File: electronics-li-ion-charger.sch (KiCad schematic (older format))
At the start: 16 parts

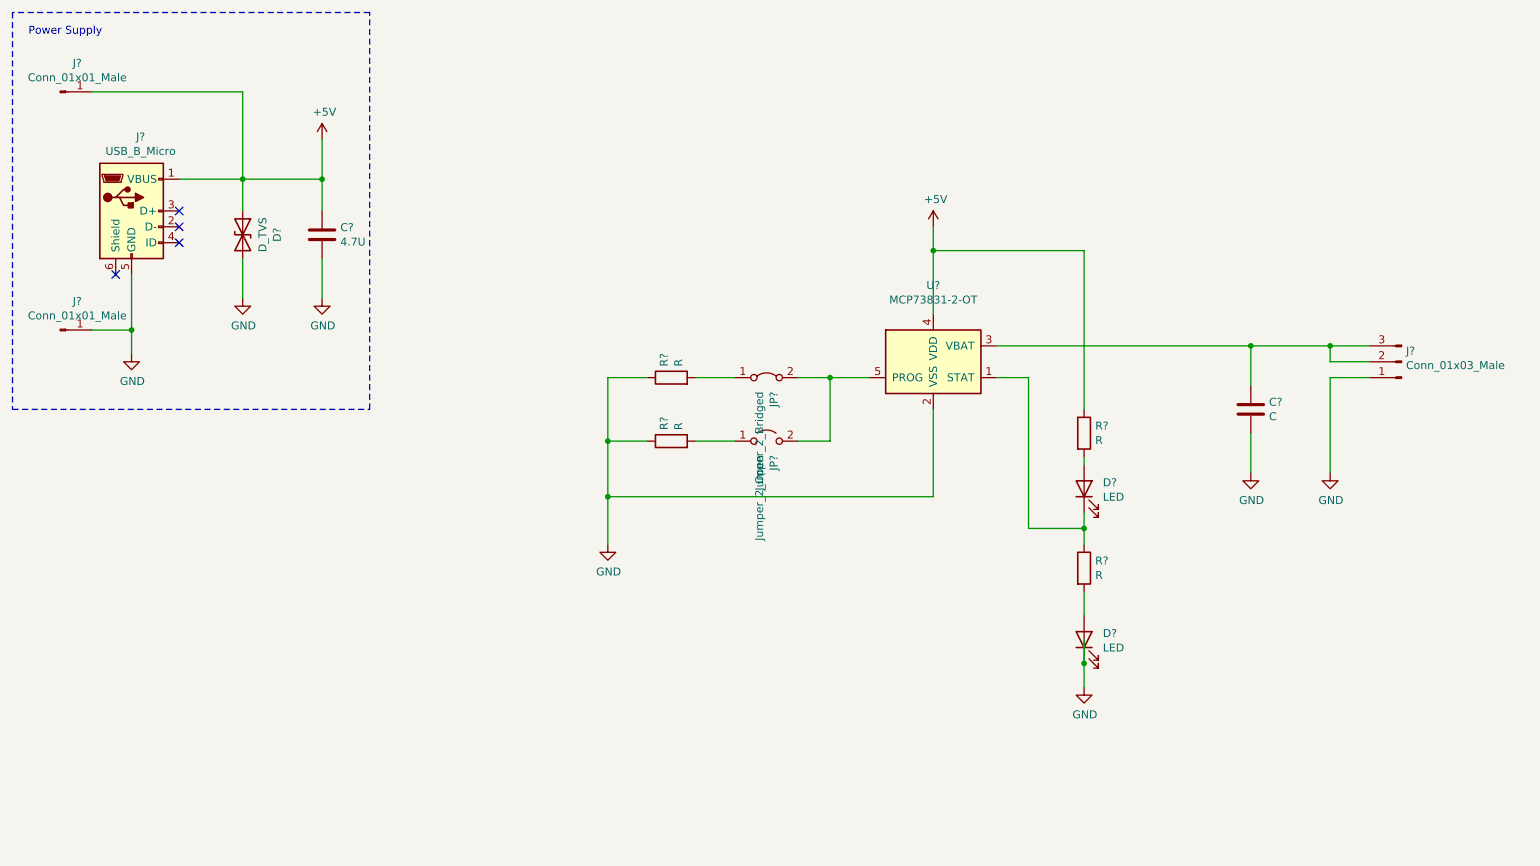
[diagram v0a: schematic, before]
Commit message: Complete charge current selection schematic.
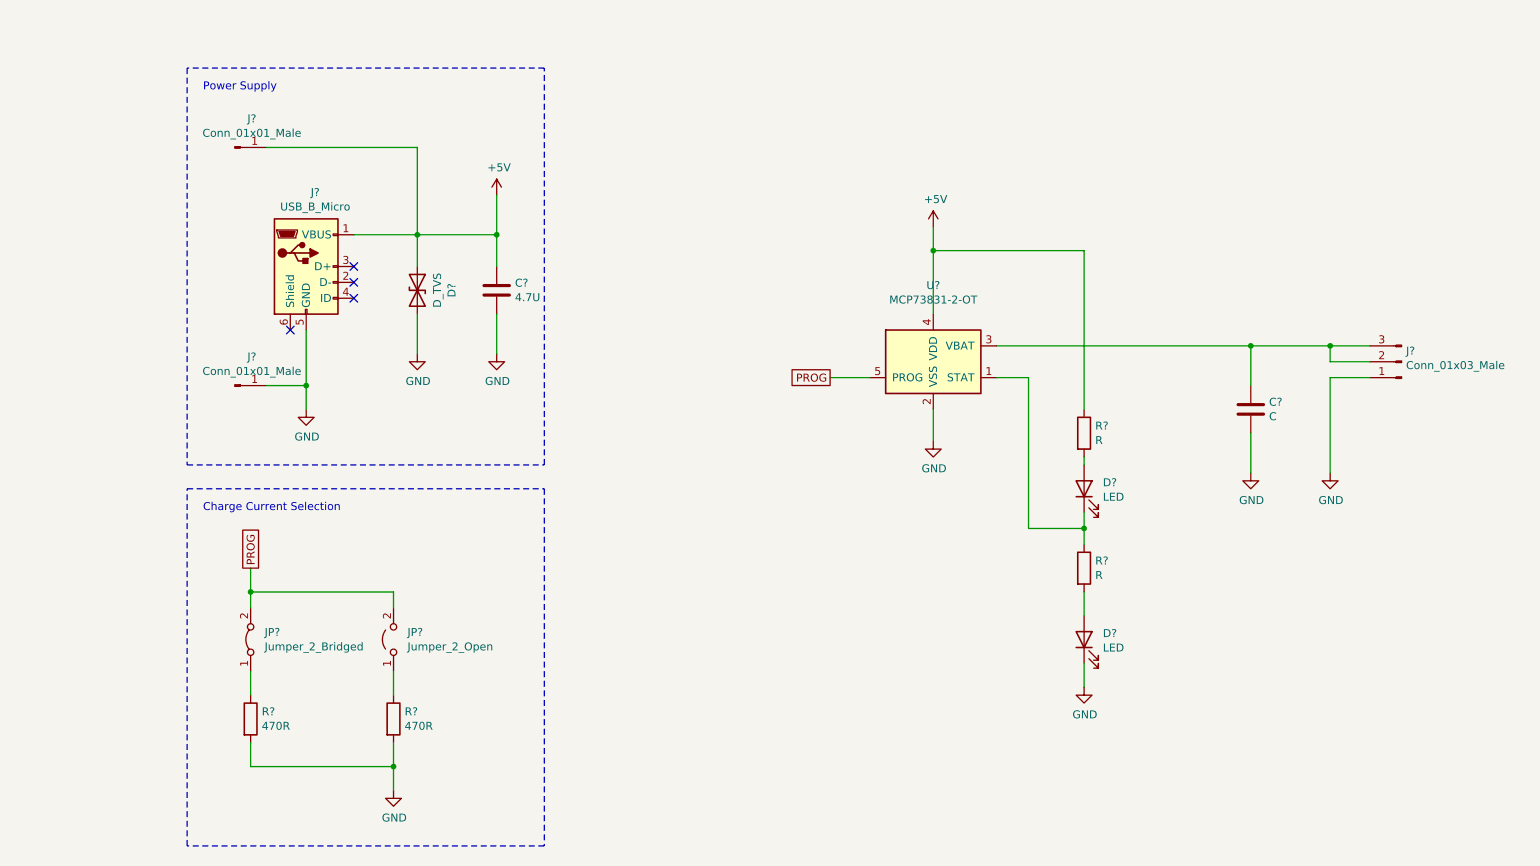
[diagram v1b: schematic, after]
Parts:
- JP? (x2): footprint (none) -> Connector_PinHeader_2.54mm:PinHeader_1x02_P2.54mm_Vertical
- R? (x2): value R -> 470R; footprint (none) -> Resistor_SMD:R_1206_3216Metric_Pad1.30x1.75mm_HandSolder
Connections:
- net GND: now also R?.2, R?.2; no longer R?.1, R?.1
- net at JP?.1 (A): now also R?.1; no longer R?.2 (x2)
- net PROG: now reaches JP?.2 (B), JP?.2 (B), U?.5 (PROG)
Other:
- note added: "Charge Current Selection"
- moved on the sheet: C?, D?, J?, JP?, R?

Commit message: Complete status LED schematic.
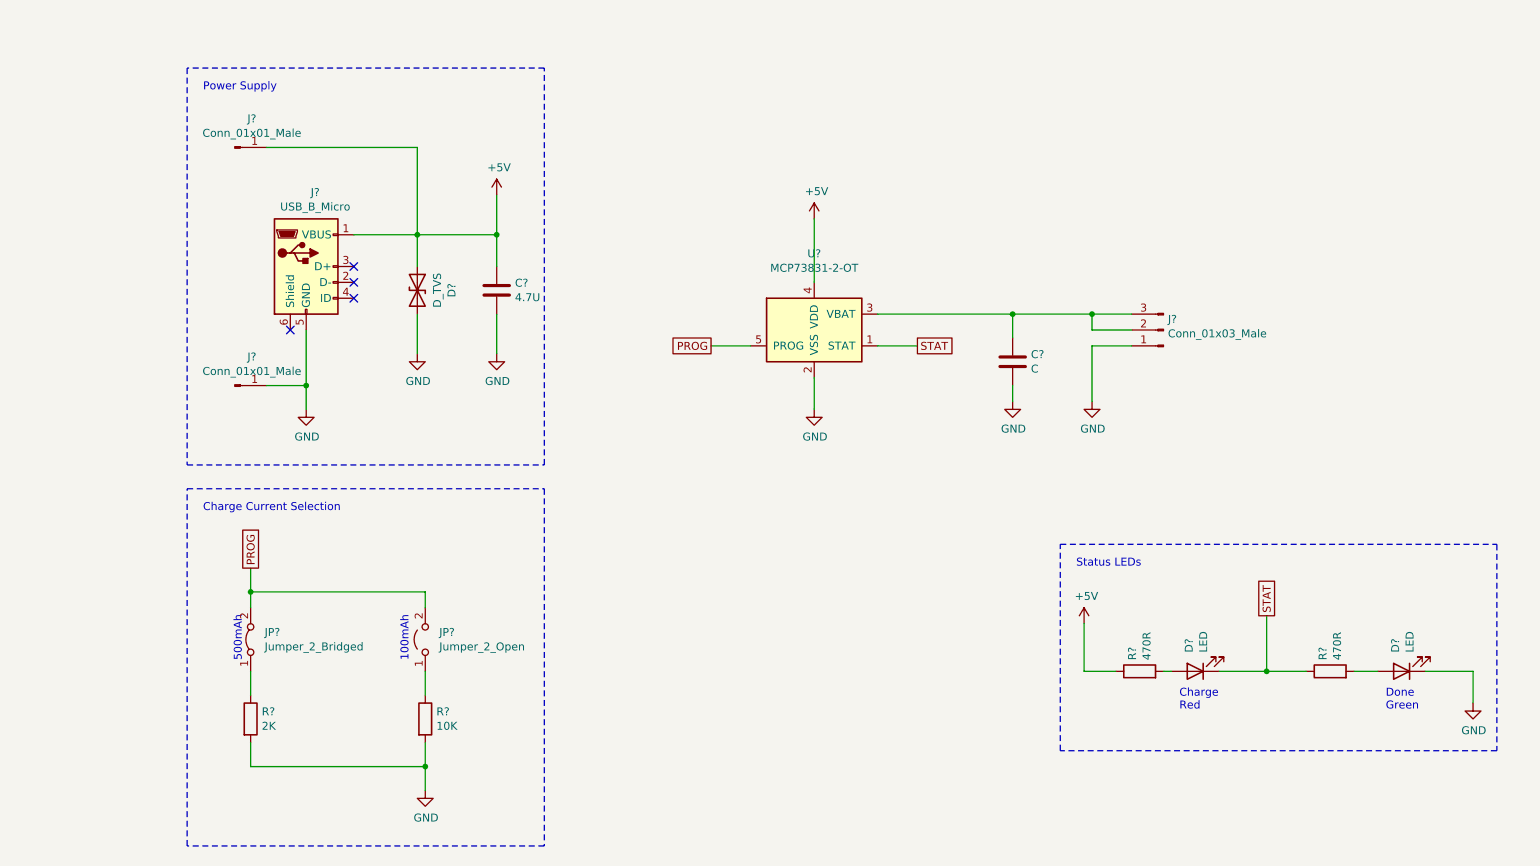
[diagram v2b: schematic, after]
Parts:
- D? (x2): footprint (none) -> LED_SMD:LED_1206_3216Metric_Pad1.42x1.75mm_HandSolder
- R? (x2): value R -> 470R; footprint (none) -> Resistor_SMD:R_1206_3216Metric_Pad1.30x1.75mm_HandSolder
- R?: value 470R -> 10K
- R?: value 470R -> 2K
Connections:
- net STAT: now reaches D?.1 (K), R?.1, U?.1 (STAT)
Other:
- note added: "100mAh"
- note added: "500mAh"
- note added: "Charge\nRed"
- note added: "Done\nGreen"
- note added: "Status LEDs"
- moved on the sheet: C?, D?, J?, JP?, R?, U?

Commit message: Complete schematic.
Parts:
- C?: value C -> 4.7U; footprint (none) -> Capacitor_SMD:C_1206_3216Metric_Pad1.33x1.80mm_HandSolder
- J?: footprint (none) -> Connector_PinHeader_2.54mm:PinHeader_1x03_P2.54mm_Vertical
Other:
- note added: "Battery Charger"
- note added: "To Battery"
- moved on the sheet: C?, D?, J?, JP?, R?, U?

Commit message: Create and assign TVS diode layout.
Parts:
- D1: renamed from D?; footprint (none) -> electronics-li-ion-charger:Diode_TVS-MSP5.0A; symbol Device:D_TVS -> Device:D_Zener
- U1: renamed from U?; footprint Package_TO_SOT_SMD:SOT-23-5 -> Package_TO_SOT_SMD:SOT-23-5_HandSoldering
- gave numbers to parts that had none: 14
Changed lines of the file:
@@
 $EndDescr
 $Comp
-L Device:R R?
+L Device:R R4
 U 1 1 5FFB4EF8
 P 6800 4950
-F 0 "R?" H 6870 4996 50  0000 L CNN
+F 0 "R4" H 6870 4996 50  0000 L CNN
 F 1 "470R" H 6870 4905 50  0000 L CNN
 F 2 "Resistor_SMD:R_1206_3216Metric_Pad1.30x1.75mm_HandSolder" V 6730 4950 50  0001 C CNN
@@
 $EndComp
 $Comp
-L Device:R R?
+L Device:R R3
 U 1 1 5FFB5567
 P 5600 4950
-F 0 "R?" H 5670 4996 50  0000 L CNN
+F 0 "R3" H 5670 4996 50  0000 L CNN
 F 1 "470R" H 5670 4905 50  0000 L CNN
 F 2 "Resistor_SMD:R_1206_3216Metric_Pad1.30x1.75mm_HandSolder" V 5530 4950 50  0001 C CNN
@@
 $EndComp
 $Comp
-L Device:C C?
+L Device:C C2
 U 1 1 5FFB5FE0
 P 7350 3400
-F 0 "C?" H 7465 3446 50  0000 L CNN
+F 0 "C2" H 7465 3446 50  0000 L CNN
 F 1 "4.7U" H 7465 3355 50  0000 L CNN
 F 2 "Capacitor_SMD:C_1206_3216Metric_Pad1.33x1.80mm_HandSolder" H 7388 3250 50  0001 C CNN
@@
 $EndComp
 $Comp
-L Device:C C?
+L Device:C C1
 U 1 1 5FFB68A7
 P 4600 2900
-F 0 "C?" H 4715 2946 50  0000 L CNN
+F 0 "C1" H 4715 2946 50  0000 L CNN
 F 1 "4.7U" H 4715 2855 50  0000 L CNN
 F 2 "Capacitor_SMD:C_1206_3216Metric_Pad1.33x1.80mm_HandSolder" H 4638 2750 50  0001 C CNN
@@
 $EndComp
 $Comp
-L Device:LED D?
+L Device:LED D3
 U 1 1 5FFB6F7B
 P 7150 4950
-F 0 "D?" V 7189 4832 50  0000 R CNN
+F 0 "D3" V 7189 4832 50  0000 R CNN
 F 1 "LED" V 7098 4832 50  0000 R CNN
 F 2 "LED_SMD:LED_1206_3216Metric_Pad1.42x1.75mm_HandSolder" H 7150 4950 50  0001 C CNN
@@
 $EndComp
 $Comp
-L Device:LED D?
+L Device:LED D2
 U 1 1 5FFB7C3E
 P 5950 4950
-F 0 "D?" V 5989 4832 50  0000 R CNN
+F 0 "D2" V 5989 4832 50  0000 R CNN
 F 1 "LED" V 5898 4832 50  0000 R CNN
 F 2 "LED_SMD:LED_1206_3216Metric_Pad1.42x1.75mm_HandSolder" H 5950 4950 50  0001 C CNN
@@
 $EndComp
 $Comp
-L Connector:USB_B_Micro J?
+L Connector:USB_B_Micro J3
 U 1 1 5FFB82FD
 P 3400 2750
-F 0 "J?" H 3457 3217 50  0000 C CNN
+F 0 "J3" H 3457 3217 50  0000 C CNN
 F 1 "USB_B_Micro" H 3457 3126 50  0000 C CNN
 F 2 "Connector_USB:USB_Micro-B_Amphenol_10118194_Horizontal" H 3550 2700 50  0001 C CNN
@@
 $EndComp
 $Comp
-L Battery_Management:MCP73831-2-OT U?
+L Battery_Management:MCP73831-2-OT U1
 U 1 1 5FFB91CD
 P 6100 3200
-F 0 "U?" H 6100 3681 50  0000 C CNN
+F 0 "U1" H 6100 3681 50  0000 C CNN
 F 1 "MCP73831-2-OT" H 6100 3590 50  0000 C CNN
-F 2 "Package_TO_SOT_SMD:SOT-23-5" H 6150 2950 50  0001 L CIN
+F 2 "Package_TO_SOT_SMD:SOT-23-5_HandSoldering" H 6150 2950 50  0001 L CIN
 F 3 "http://ww1.microchip.com/downloads/en/DeviceDoc/20001984g.pdf" H 5950 3150 50  0001 C CNN
 	1    6100 3200
@@
 $EndComp
 $Comp
-L Device:D_TVS D?
+L Device:D_Zener D1
 U 1 1 5FFBBF19
 P 4100 2900
-F 0 "D?" H 4100 3117 50  0000 C CNN
+F 0 "D1" H 4100 3117 50  0000 C CNN
 F 1 "D_TVS" H 4100 3026 50  0000 C CNN
-F 2 "" H 4100 2900 50  0001 C CNN
+F 2 "electronics-li-ion-charger:Diode_TVS-MSP5.0A" H 4100 2900 50  0001 C CNN
 F 3 "~" H 4100 2900 50  0001 C CNN
 	1    4100 2900
@@
 $EndComp
 $Comp
-L Connector:Conn_01x03_Male J?
+L Connector:Conn_01x03_Male J4
 U 1 1 5FFBF742
 P 8300 3200
-F 0 "J?" H 8272 3132 50  0000 R CNN
+F 0 "J4" H 8272 3132 50  0000 R CNN
 F 1 "Conn_01x03_Male" H 8272 3223 50  0000 R CNN
 F 2 "Connector_PinHeader_2.54mm:PinHeader_1x03_P2.54mm_Vertical" H 8300 3200 50  0001 C CNN
@@
 L power:GND #PWR0106
 U 1 1 5FFE4565
-P 4100 3300
-F 0 "#PWR0106" H 4100 3050 50  0001 C CNN
-F 1 "GND" H 4105 3127 50  0000 C CNN
-F 2 "" H 4100 3300 50  0001 C CNN
-F 3 "" H 4100 3300 50  0001 C CNN
-	1    4100 3300
+P 4100 3150
+F 0 "#PWR0106" H 4100 2900 50  0001 C CNN
+F 1 "GND" H 4105 2977 50  0000 C CNN
+F 2 "" H 4100 3150 50  0001 C CNN
+F 3 "" H 4100 3150 50  0001 C CNN
+	1    4100 3150
 	1    0    0    -1
 $EndComp
@@
 L power:GND #PWR0107
 U 1 1 5FFE472B
-P 4600 3300
-F 0 "#PWR0107" H 4600 3050 50  0001 C CNN
-F 1 "GND" H 4605 3127 50  0000 C CNN
-F 2 "" H 4600 3300 50  0001 C CNN
-F 3 "" H 4600 3300 50  0001 C CNN
-	1    4600 3300
+P 4600 3150
+F 0 "#PWR0107" H 4600 2900 50  0001 C CNN
+F 1 "GND" H 4605 2977 50  0000 C CNN
+F 2 "" H 4600 3150 50  0001 C CNN
+F 3 "" H 4600 3150 50  0001 C CNN
+	1    4600 3150
 	1    0    0    -1
 $EndComp
@@
 	4100 2750 4100 2550
 Wire Wire Line
-	4100 3050 4100 3300
-Wire Wire Line
-	4600 3050 4600 3300
+	4600 3050 4600 3150
 Wire Wire Line
 	4100 2550 4600 2550
@@
 Power Supply
 $Comp
-L Connector:Conn_01x01_Male J?
+L Connector:Conn_01x01_Male J1
 U 1 1 5FFF75A8
 P 2950 2000
-F 0 "J?" H 3058 2181 50  0000 C CNN
+F 0 "J1" H 3058 2181 50  0000 C CNN
 F 1 "Conn_01x01_Male" H 3058 2090 50  0000 C CNN
 F 2 "Connector_PinHeader_2.54mm:PinHeader_1x01_P2.54mm_Vertical" H 2950 2000 50  0001 C CNN
@@
 $EndComp
 $Comp
-L Connector:Conn_01x01_Male J?
+L Connector:Conn_01x01_Male J2
 U 1 1 5FFF7E39
 P 2950 3500
-F 0 "J?" H 3058 3681 50  0000 C CNN
+F 0 "J2" H 3058 3681 50  0000 C CNN
 F 1 "Conn_01x01_Male" H 3058 3590 50  0000 C CNN
 F 2 "Connector_PinHeader_2.54mm:PinHeader_1x01_P2.54mm_Vertical" H 2950 3500 50  0001 C CNN
@@
 	4900 1500 2650 1500
 $Comp
-L Device:R R?
+L Device:R R2
 U 1 1 5FFB5769
 P 4150 5600
-F 0 "R?" H 4220 5646 50  0000 L CNN
+F 0 "R2" H 4220 5646 50  0000 L CNN
 F 1 "10K" H 4220 5555 50  0000 L CNN
 F 2 "Resistor_SMD:R_1206_3216Metric_Pad1.30x1.75mm_HandSolder" V 4080 5600 50  0001 C CNN
@@
 $EndComp
 $Comp
-L Jumper:Jumper_2_Bridged JP?
+L Jumper:Jumper_2_Bridged JP1
 U 1 1 5FFBEBFA
 P 3050 5100
-F 0 "JP?" V 3096 5012 50  0000 R CNN
+F 0 "JP1" V 3096 5012 50  0000 R CNN
 F 1 "Jumper_2_Bridged" V 3005 5012 50  0000 R CNN
 F 2 "Connector_PinHeader_2.54mm:PinHeader_1x02_P2.54mm_Vertical" H 3050 5100 50  0001 C CNN
@@
 $EndComp
 $Comp
-L Device:R R?
+L Device:R R1
 U 1 1 5FFB5B83
 P 3050 5600
-F 0 "R?" H 3120 5646 50  0000 L CNN
+F 0 "R1" H 3120 5646 50  0000 L CNN
 F 1 "2K" H 3120 5555 50  0000 L CNN
 F 2 "Resistor_SMD:R_1206_3216Metric_Pad1.30x1.75mm_HandSolder" V 2980 5600 50  0001 C CNN
@@
 	6950 4950 7000 4950
 $Comp
-L power:GND #PWR?
+L power:GND #PWR02
 U 1 1 6001F8A6
 P 6100 3700
-F 0 "#PWR?" H 6100 3450 50  0001 C CNN
+F 0 "#PWR02" H 6100 3450 50  0001 C CNN
 F 1 "GND" H 6105 3527 50  0000 C CNN
 F 2 "" H 6100 3700 50  0001 C CNN
@@
 	4150 5900 4150 5750
 $Comp
-L Jumper:Jumper_2_Open JP?
+L Jumper:Jumper_2_Open JP2
 U 1 1 5FFBE0EB
 P 4150 5100
-F 0 "JP?" V 4196 5012 50  0000 R CNN
+F 0 "JP2" V 4196 5012 50  0000 R CNN
 F 1 "Jumper_2_Open" V 4105 5012 50  0000 R CNN
 F 2 "Connector_PinHeader_2.54mm:PinHeader_1x02_P2.54mm_Vertical" H 4150 5100 50  0001 C CNN
@@
 	6100 2500 6100 2900
 $Comp
-L power:+5V #PWR?
+L power:+5V #PWR01
 U 1 1 60047041
 P 5250 4650
-F 0 "#PWR?" H 5250 4500 50  0001 C CNN
+F 0 "#PWR01" H 5250 4500 50  0001 C CNN
 F 1 "+5V" H 5265 4823 50  0000 C CNN
 F 2 "" H 5250 4650 50  0001 C CNN
@@
 Text Notes 8150 2950 0    50   ~ 0
 To Battery
+Wire Wire Line
+	4100 3050 4100 3150
 $EndSCHEMATC

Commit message: Draft PCB layout.
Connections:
- net +5V: now also D2.2 (A); no longer R3.1
- net STAT: now also R3.2; no longer D2.1 (K)
- net VBAT: now reaches C2.1, J4.2 (Pin_2), J4.3 (Pin_3), U1.3 (VBAT)
- new net: D2.1 (K), R3.1
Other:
- moved on the sheet: D2, R3
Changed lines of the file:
@@
 L Device:R R3
 U 1 1 5FFB5567
-P 5600 4950
-F 0 "R3" H 5670 4996 50  0000 L CNN
-F 1 "470R" H 5670 4905 50  0000 L CNN
-F 2 "Resistor_SMD:R_1206_3216Metric_Pad1.30x1.75mm_HandSolder" V 5530 4950 50  0001 C CNN
-F 3 "~" H 5600 4950 50  0001 C CNN
-	1    5600 4950
+P 6000 4950
+F 0 "R3" H 6070 4996 50  0000 L CNN
+F 1 "470R" H 6070 4905 50  0000 L CNN
+F 2 "Resistor_SMD:R_1206_3216Metric_Pad1.30x1.75mm_HandSolder" V 5930 4950 50  0001 C CNN
+F 3 "~" H 6000 4950 50  0001 C CNN
+	1    6000 4950
 	0    -1   -1   0
 $EndComp
@@
 L Device:LED D2
 U 1 1 5FFB7C3E
-P 5950 4950
-F 0 "D2" V 5989 4832 50  0000 R CNN
-F 1 "LED" V 5898 4832 50  0000 R CNN
-F 2 "LED_SMD:LED_1206_3216Metric_Pad1.42x1.75mm_HandSolder" H 5950 4950 50  0001 C CNN
-F 3 "~" H 5950 4950 50  0001 C CNN
-	1    5950 4950
+P 5600 4950
+F 0 "D2" V 5639 4832 50  0000 R CNN
+F 1 "LED" V 5548 4832 50  0000 R CNN
+F 2 "LED_SMD:LED_1206_3216Metric_Pad1.42x1.75mm_HandSolder" H 5600 4950 50  0001 C CNN
+F 3 "~" H 5600 4950 50  0001 C CNN
+	1    5600 4950
 	-1   0    0    1
 $EndComp
@@
 $EndComp
 Wire Wire Line
-	5750 4950 5800 4950
+	5750 4950 5850 4950
 $Comp
 L power:GND #PWR0106
@@
 	6400 4600 6400 4950
 Wire Wire Line
-	6100 4950 6400 4950
+	6150 4950 6400 4950
 Connection ~ 6400 4950
 Wire Wire Line
@@
 Text Notes 5200 4300 0    50   ~ 0
 Status LEDs
-Text Notes 5850 5200 0    50   ~ 0
+Text Notes 5500 5200 0    50   ~ 0
 Charge\nRed
-Text Notes 7150 5200 0    50   ~ 0
+Text Notes 7100 5200 0    50   ~ 0
 Done\nGreen
 Wire Notes Line
@@
 Wire Wire Line
 	4100 3050 4100 3150
+Text Label 6850 3100 0    50   ~ 0
+VBAT
 $EndSCHEMATC
